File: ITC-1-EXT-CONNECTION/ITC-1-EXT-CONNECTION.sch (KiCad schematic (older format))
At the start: 10 parts

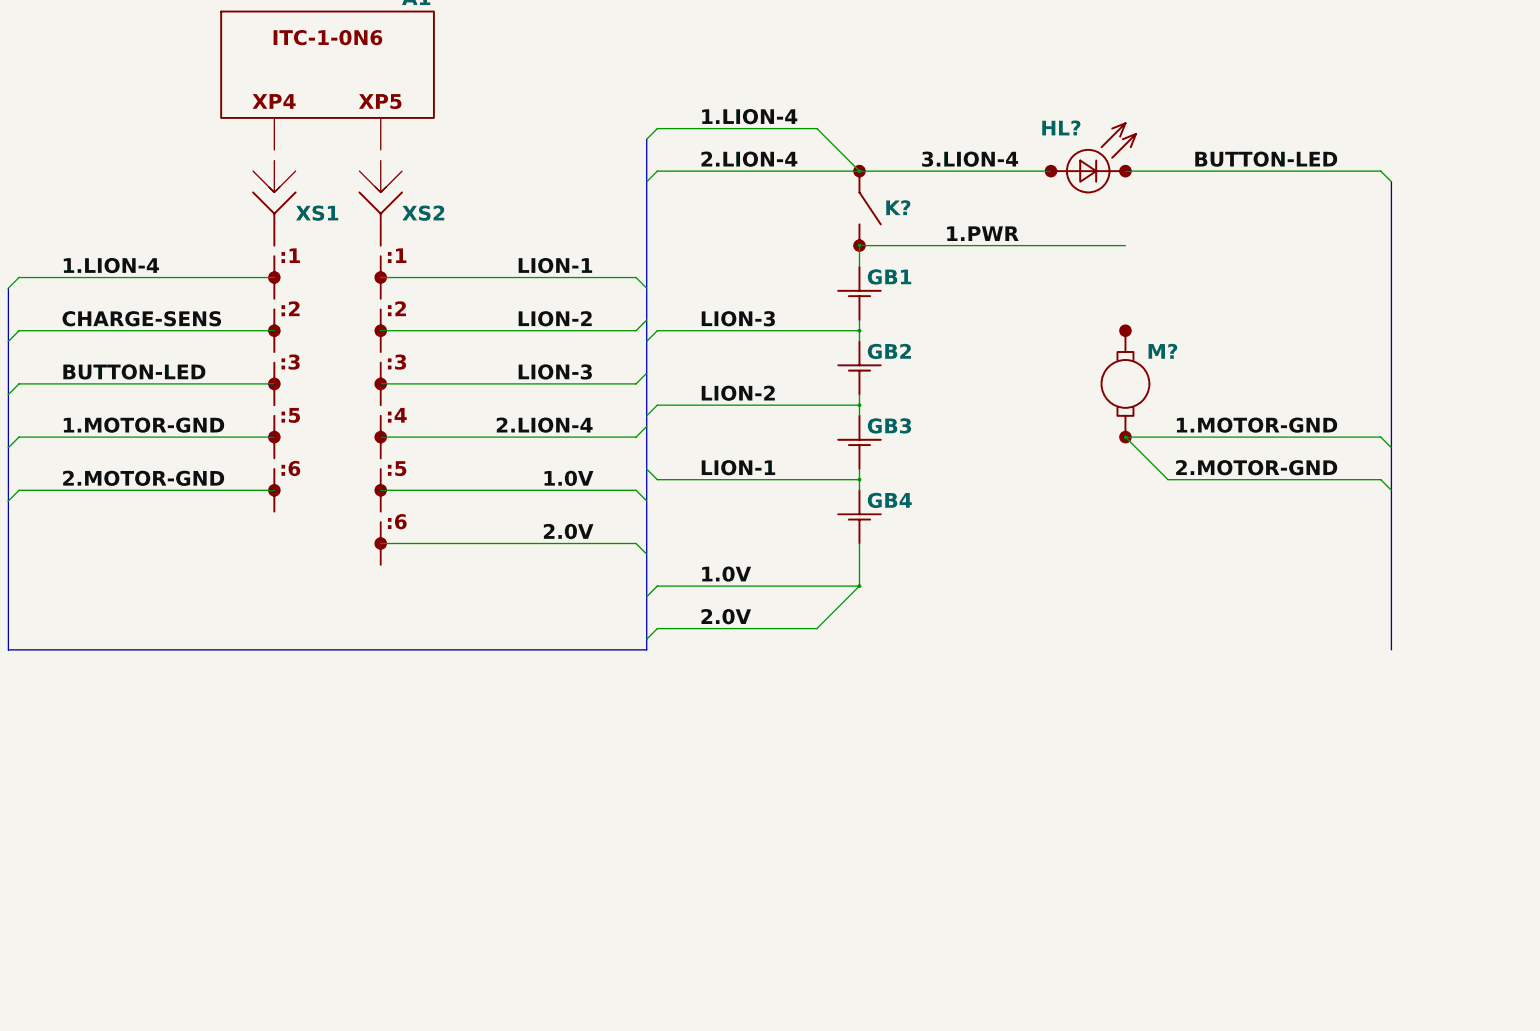
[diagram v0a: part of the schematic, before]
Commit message: подготовлена схема внешних подключений
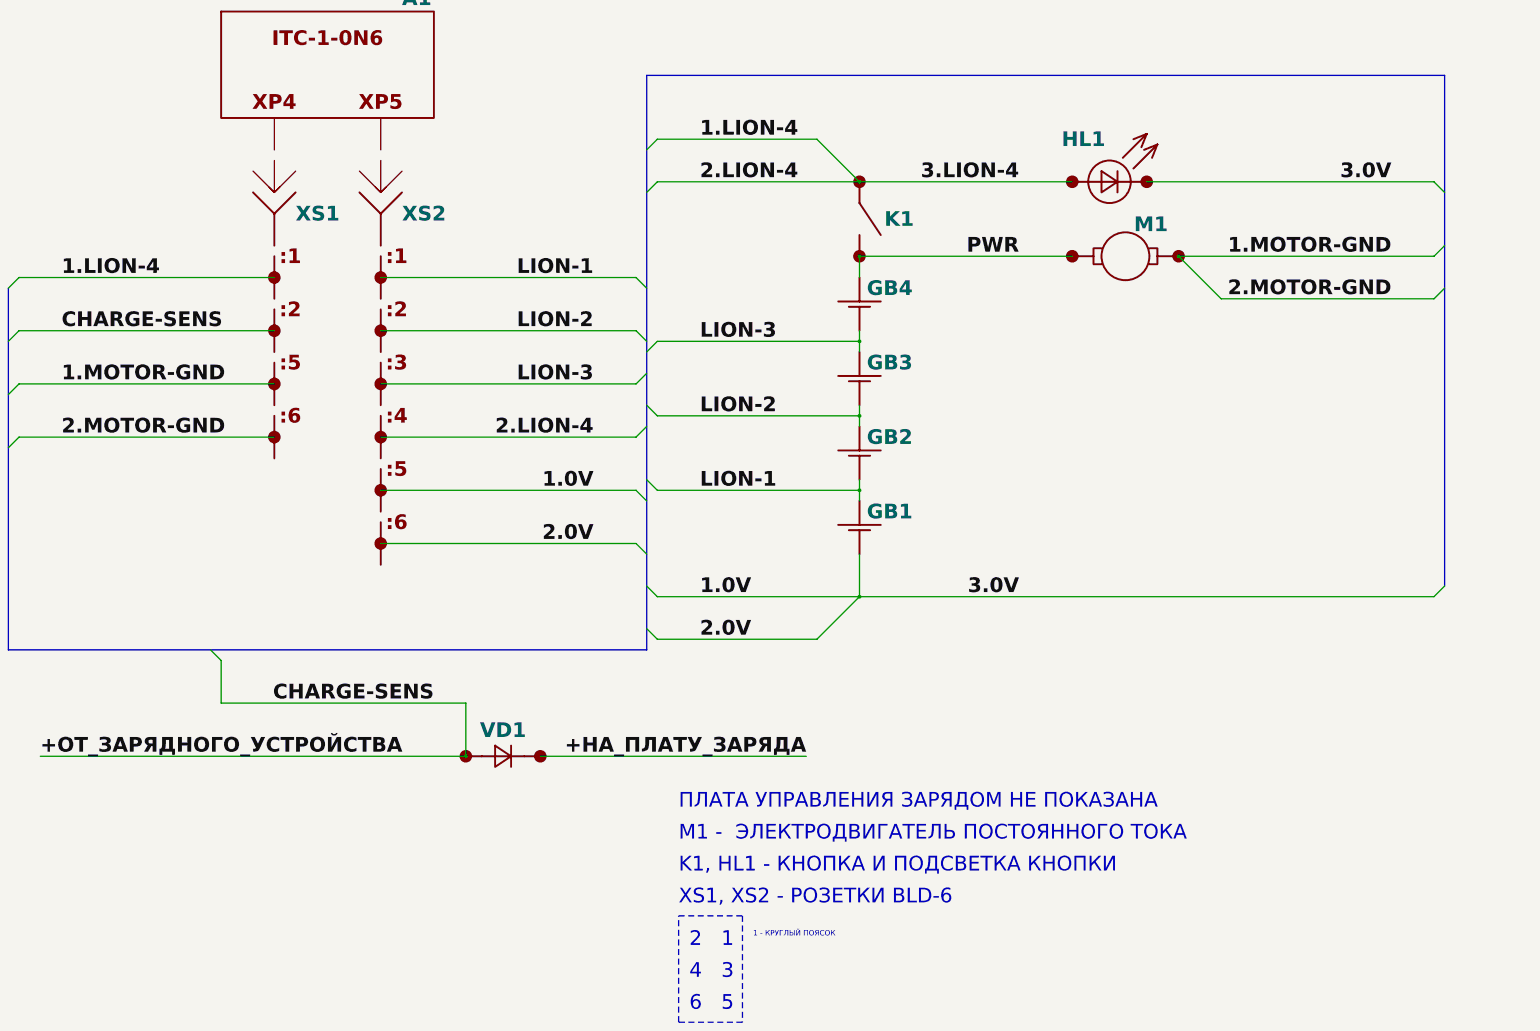
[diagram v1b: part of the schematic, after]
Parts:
- removed XS1: Розетка_BLD-6#N4, symbol BIG_schemes:Розетка_BLD-6#N4
- added VD1: Диод_кремниевый, symbol BIG_schemes:Диод_кремниевый
- added XS1: Розетка_BLD-6#N3N4, symbol BIG_schemes:Розетка_BLD-6#N3N4
- gave numbers to parts that had none: 3
- renumbered GB4 to GB1, GB3 to GB2, GB2 to GB3, GB1 to GB4
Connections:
- net 1.PWR is gone; now on net PWR: GB4.+, K1.2
- net BUTTON-LED is gone; now on net 1.0V: HL1.K
- net 1.LION-4: now also XS1.1
- net 1.MOTOR-GND: now also XS1.5, XS1.6
- net PWR: now reaches M1.1
- new net +НА_ПЛАТУ_ЗАРЯДА: VD1.K
- new net +ОТ_ЗАРЯДНОГО_УСТРОЙСТВА: VD1.A, XS1.2
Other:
- note added: "1"
- note added: "1 - КРУГЛЫЙ ПОЯСОК"
- note added: "2"
- note added: "3"
- note added: "4"
- note added: "5"
- note added: "6"
- note added: "K1, HL1 - КНОПКА И ПОДСВЕТКА КНОПКИ"
- note added: "M1 - ЭЛЕКТРОДВИГАТЕЛЬ ПОСТОЯННОГО ТОКА"
- note added: "XS1, XS2 - РОЗЕТКИ BLD-6"
- note added: "ПЛАТА УПРАВЛЕНИЯ ЗАРЯДОМ НЕ ПОКАЗАНА"
- moved on the sheet: GB1, GB2, GB3, GB4, HL1, K1, M1

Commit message: arduino: задержка запуска и выключение по таймауту
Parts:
- removed A1: ITC-1-0N6, symbol BIG_schemes:ITC-1-0N6
- removed XS1: Розетка_BLD-6#N3N4, symbol BIG_schemes:Розетка_BLD-6#N3N4
- removed XS2: Розетка_BLD-6#0, symbol BIG_schemes:Розетка_BLD-6#0
- added A?: ITC-1-0N6&1, symbol BIG_schemes:ITC-1-0N6&1
- added VD?: Диод_кремниевый, symbol BIG_schemes:Диод_кремниевый
- added XP? (x10): Вилка_ножевая, symbol BIG_schemes:Вилка_ножевая
- added XS? (x10): Розетка_ножевая, symbol BIG_schemes:Розетка_ножевая
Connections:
- net +ОТ_ЗАРЯДНОГО_УСТРОЙСТВА: now also A?.2
- net 1.0V: now also A?.5, A?.6, XP?.1; no longer GB1.-, HL1.K
- net 1.MOTOR-GND: now also A?.5, A?.6, XS?.1; no longer M1.1
- net 1.LION-4: no longer names the net of HL1.A, K1.1
- net 1.LION-4: now also XS?.1
- net LION-1 renamed B
- net B: now also XS?.1
- net LION-2 renamed B.LI-2
- net B.LI-2: now also XS?.1
- net LION-3 renamed B.LI-3
- net B.LI-3: now also XS?.1
- removed net PWR: GB4.+, K1.2, M1.1
- new net: HL1.K, XP?.1
- new net: K1.2, XP?.1
- new net 3.0V: GB1.-, XS?.1, XS?.1
- new net B+: GB4.+, XS?.1
- new net B2.LI-4: XP?.1, XS?.1, XS?.1
- new net LI-1: A?.1, XP?.1
- new net LI-2: A?.2, XP?.1
- new net LI-3: A?.3, XP?.1
- new net LI-4: A?.4, XP?.1
- new net M1+: M1.1, VD?.K, XP?.1
- new net M1-: M1.1, VD?.A, XP?.1
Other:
- note added: "НА BMS"
- moved on the sheet: GB1, GB2, GB3, GB4, HL1, K1, M1, VD1

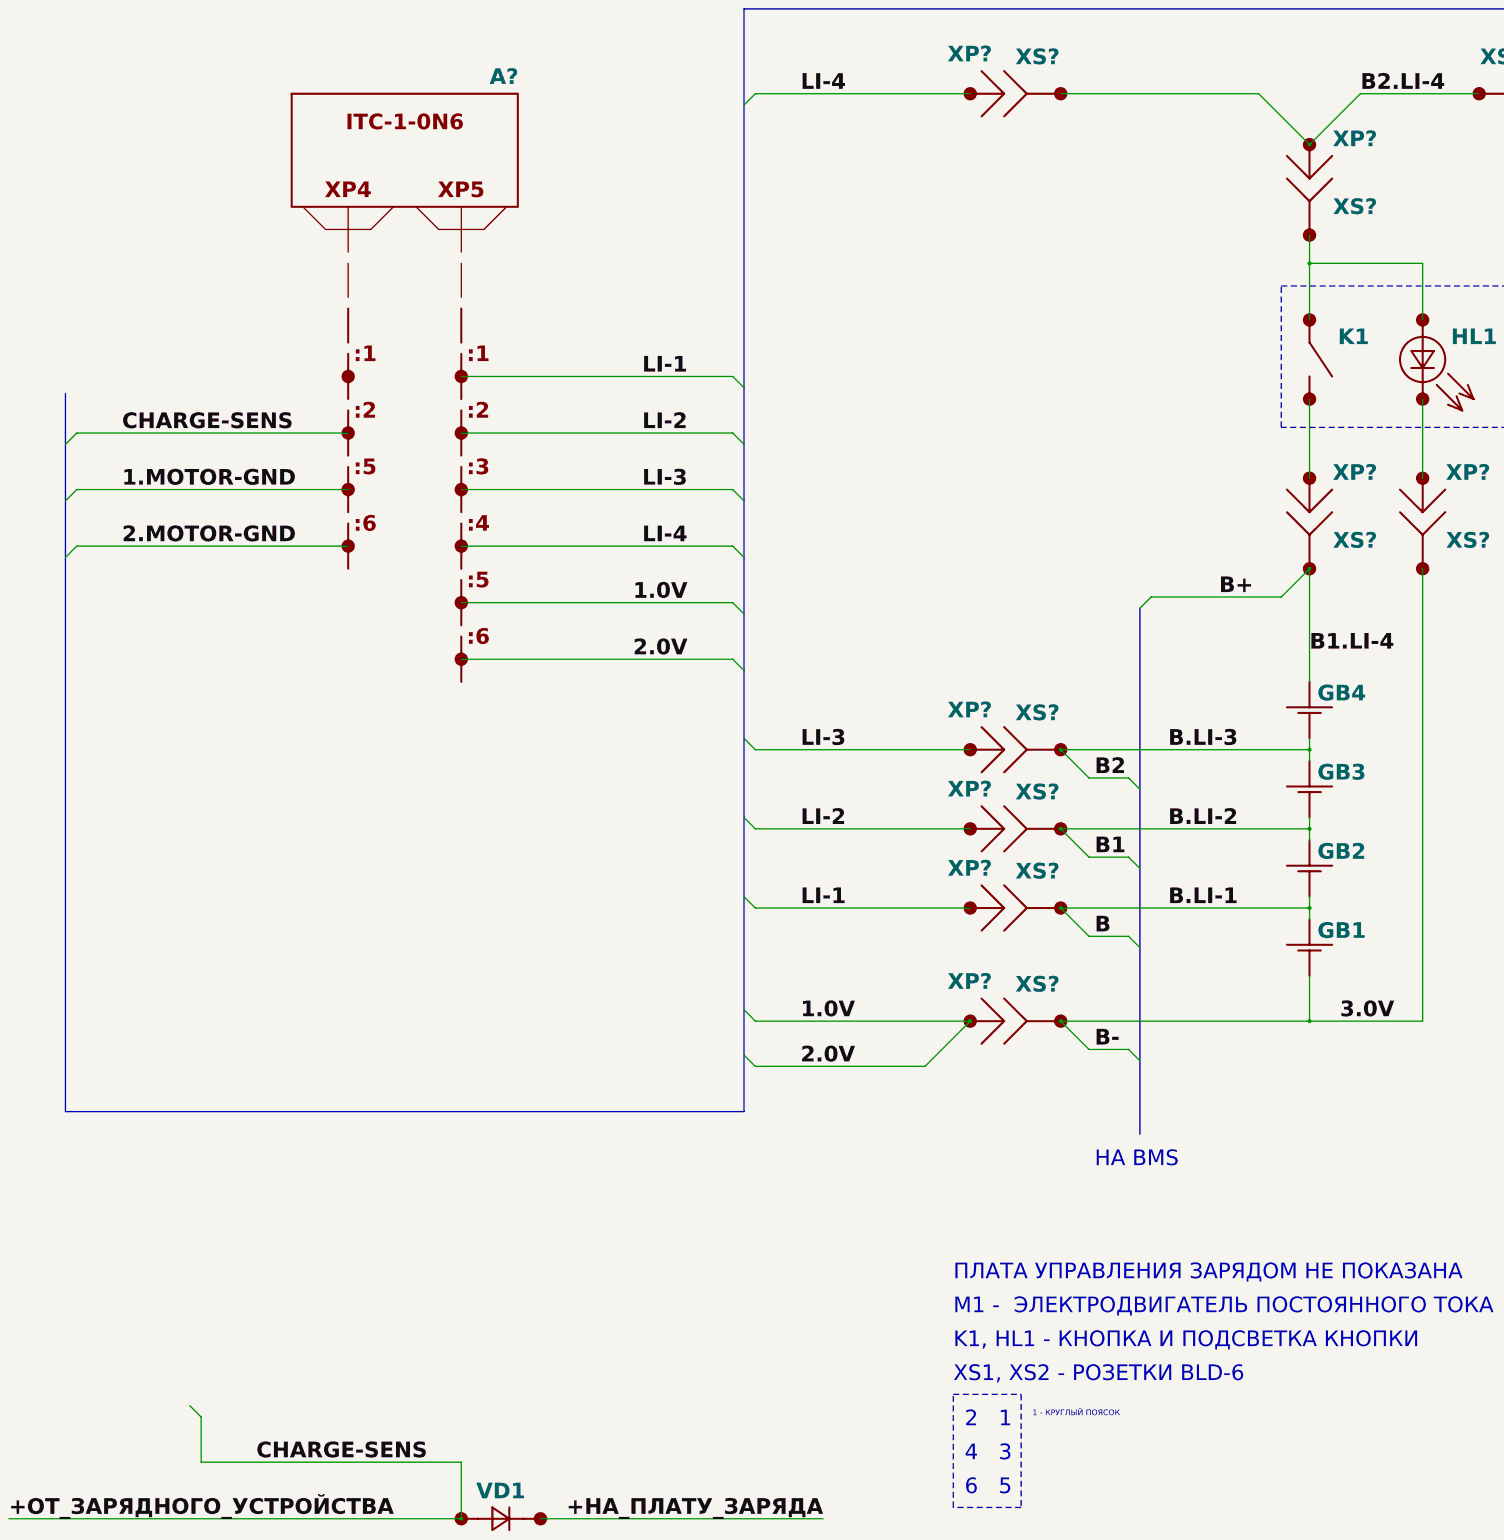
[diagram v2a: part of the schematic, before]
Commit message: обновлено УГО для внешнего подключения
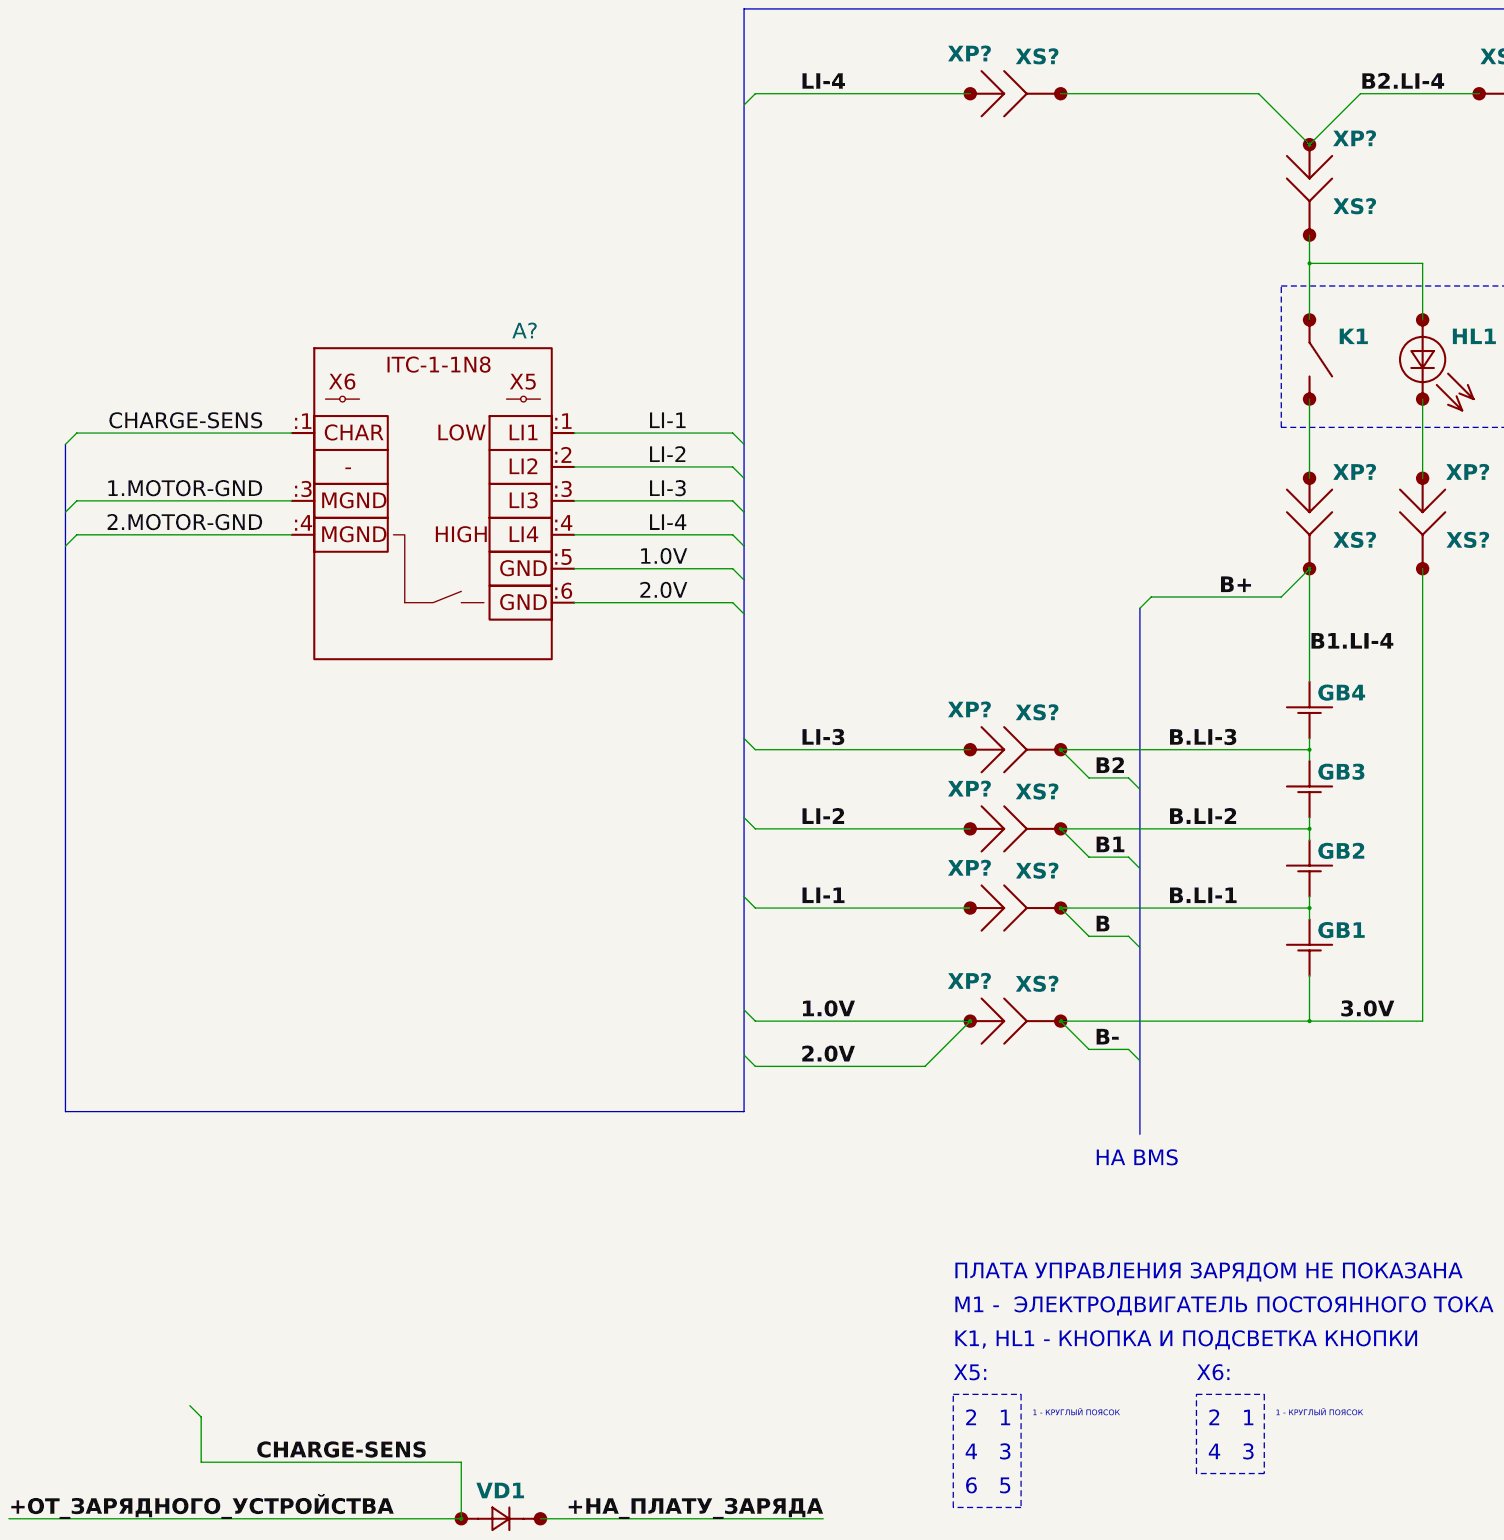
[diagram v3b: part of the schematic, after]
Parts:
- removed A?: ITC-1-0N6&1, symbol BIG_schemes:ITC-1-0N6&1
- added A?: ITC-1-1N8&1, symbol BIG_schemes:ITC-1-1N8&1
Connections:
- net +ОТ_ЗАРЯДНОГО_УСТРОЙСТВА: now also A?.1A
- net 1.0V: now also A?.5B, A?.6B
- net 1.MOTOR-GND: now also A?.3A, A?.4A
- net LI-1: now also A?.1B
- net LI-2: now also A?.2B
- net LI-3: now also A?.3B
- net LI-4: now also A?.4B
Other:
- note added: "X5:"
- note added: "X6:"
- note removed: "XS1, XS2 - РОЗЕТКИ BLD-6"
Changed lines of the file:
@@
 EESchema Schematic File Version 4
-LIBS:ITC-1-EXT-CONNECTION-cache
-EELAYER 29 0
+EELAYER 30 0
 EELAYER END
 $Descr A2 23386 16535
@@
 Comment4 ""
 $EndDescr
-Text Label 2000 5500 0    138  ~ 28
+Text Label 3250 5500 2    138  ~ 0
 CHARGE-SENS
-Text Label 2000 6000 0    138  ~ 28
+Text Label 3250 6100 2    138  ~ 0
 1.MOTOR-GND
-Text Label 2000 6500 0    138  ~ 28
+Text Label 3250 6400 2    138  ~ 0
 2.MOTOR-GND
-Text Label 7000 5000 2    138  ~ 28
+Text Label 7000 5500 2    138  ~ 0
 LI-1
-Text Label 7000 5500 2    138  ~ 28
+Text Label 7000 5800 2    138  ~ 0
 LI-2
-Text Label 7000 6000 2    138  ~ 28
+Text Label 7000 6100 2    138  ~ 0
 LI-3
-Text Label 7000 6500 2    138  ~ 28
+Text Label 7000 6400 2    138  ~ 0
 LI-4
-Text Label 7000 7000 2    138  ~ 28
+Text Label 7000 6700 2    138  ~ 0
 1.0V
-Text Label 7000 7500 2    138  ~ 28
+Text Label 7000 7000 2    138  ~ 0
 2.0V
 Text Label 8000 9000 0    138  ~ 28
@@
 	1500 5600 1600 5500
 Entry Wire Line
-	1500 6100 1600 6000
-Entry Wire Line
-	1500 6600 1600 6500
-Wire Wire Line
-	1600 5500 4000 5500
-Wire Wire Line
-	1600 6000 4000 6000
-Wire Wire Line
-	1600 6500 4000 6500
+	1500 6200 1600 6100
+Entry Wire Line
+	1500 6500 1600 6400
+Wire Wire Line
+	1600 5500 3500 5500
+Wire Wire Line
+	1600 6100 3500 6100
+Wire Wire Line
+	1600 6400 3500 6400
 $Comp
 L BIG_schemes:Аккумулятор GB4
@@
 $EndComp
 Entry Wire Line
-	7400 5000 7500 5100
-Entry Wire Line
 	7400 5500 7500 5600
 Entry Wire Line
-	7500 6100 7400 6000
-Entry Wire Line
-	7500 6600 7400 6500
+	7400 5800 7500 5900
+Entry Wire Line
+	7500 6200 7400 6100
+Entry Wire Line
+	7500 6500 7400 6400
+Entry Wire Line
+	7400 6700 7500 6800
 Entry Wire Line
 	7400 7000 7500 7100
-Entry Wire Line
-	7400 7500 7500 7600
 Wire Wire Line
 	9500 2500 7600 2500
@@
 1 - КРУГЛЫЙ ПОЯСОК
 Text Notes 9350 13900 0    138  ~ 0
-XS1, XS2 - РОЗЕТКИ BLD-6
+X5:
 Text Label 13250 10700 2    138  ~ 28
 3.0V
@@
 Wire Wire Line
 	10300 10700 12500 10700
-$Comp
-L BIG_schemes:ITC-1-0N6&1 A?
-U 1 1 611BFE40
-P 4000 3500
-F 0 "A?" H 5250 4650 138 0000 L CNB
-F 1 "ITC-1-0N6&1" H 4500 4650 50  0001 C CNB
-F 2 "" H 3500 4500 50  0001 C CNN
-F 3 "" H 3500 4500 50  0001 C CNN
-	1    4000 3500
-	1    0    0    -1
-$EndComp
 Wire Wire Line
 	12500 6700 12250 6950
@@
 B1.LI-4
 Wire Wire Line
-	5000 5000 7400 5000
-Wire Wire Line
-	5000 5500 7400 5500
-Wire Wire Line
-	5000 6000 7400 6000
-Wire Wire Line
-	5000 6500 7400 6500
-Wire Wire Line
-	5000 7000 7400 7000
-Wire Wire Line
-	5000 7500 7400 7500
+	6000 5500 7400 5500
+Wire Wire Line
+	6000 5800 7400 5800
+Wire Wire Line
+	6000 6100 7400 6100
+Wire Wire Line
+	6000 6400 7400 6400
+Wire Wire Line
+	6000 6700 7400 6700
+Wire Wire Line
+	6000 7000 7400 7000
 $Comp
 L BIG_schemes:Диод_кремниевый VD?
@@
 B2.LI-4
 Connection ~ 12500 2950
+Text Notes 10600 12000 0    138  ~ 0
+НА BMS
+$Comp
+L BIG_schemes:ITC-1-1N8&1 A?
+U 1 1 61EE9F7A
+P 3500 5500
+F 0 "A?" H 5450 6400 138 0000 L CNN
+F 1 "ITC-1-1N8&1" H 4800 3600 50  0001 C CNB
+F 2 "" H -550 8400 50  0001 C CNN
+F 3 "" H -550 8400 50  0001 C CNN
+	1    3500 5500
+	1    0    0    -1
+$EndComp
+Text Notes 11900 14300 0    138  ~ 0
+1
+Text Notes 11600 14300 0    138  ~ 0
+2
+Text Notes 11900 14600 0    138  ~ 0
+3
+Text Notes 11600 14600 0    138  ~ 0
+4
+Wire Notes Line
+	11500 14000 12100 14000
+Wire Notes Line
+	12100 14000 12100 14700
+Wire Notes Line
+	12100 14700 11500 14700
+Wire Notes Line
+	11500 14700 11500 14000
+Text Notes 12200 14200 0    50   ~ 0
+1 - КРУГЛЫЙ ПОЯСОК
+Text Notes 11500 13900 0    138  ~ 0
+X6:
 Wire Bus Line
 	21000 1750 21000 2800
 Wire Bus Line
+	1500 5600 1500 11500
+Wire Bus Line
 	11000 7050 11000 11700
 Wire Bus Line
-	1500 5150 1500 11500
-Wire Bus Line
 	7500 1750 7500 11500
-Text Notes 10600 12000 0    138  ~ 0
-НА BMS
 $EndSCHEMATC
